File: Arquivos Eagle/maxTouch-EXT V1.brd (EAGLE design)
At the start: 35.6 x 53.3 mm, 14 parts

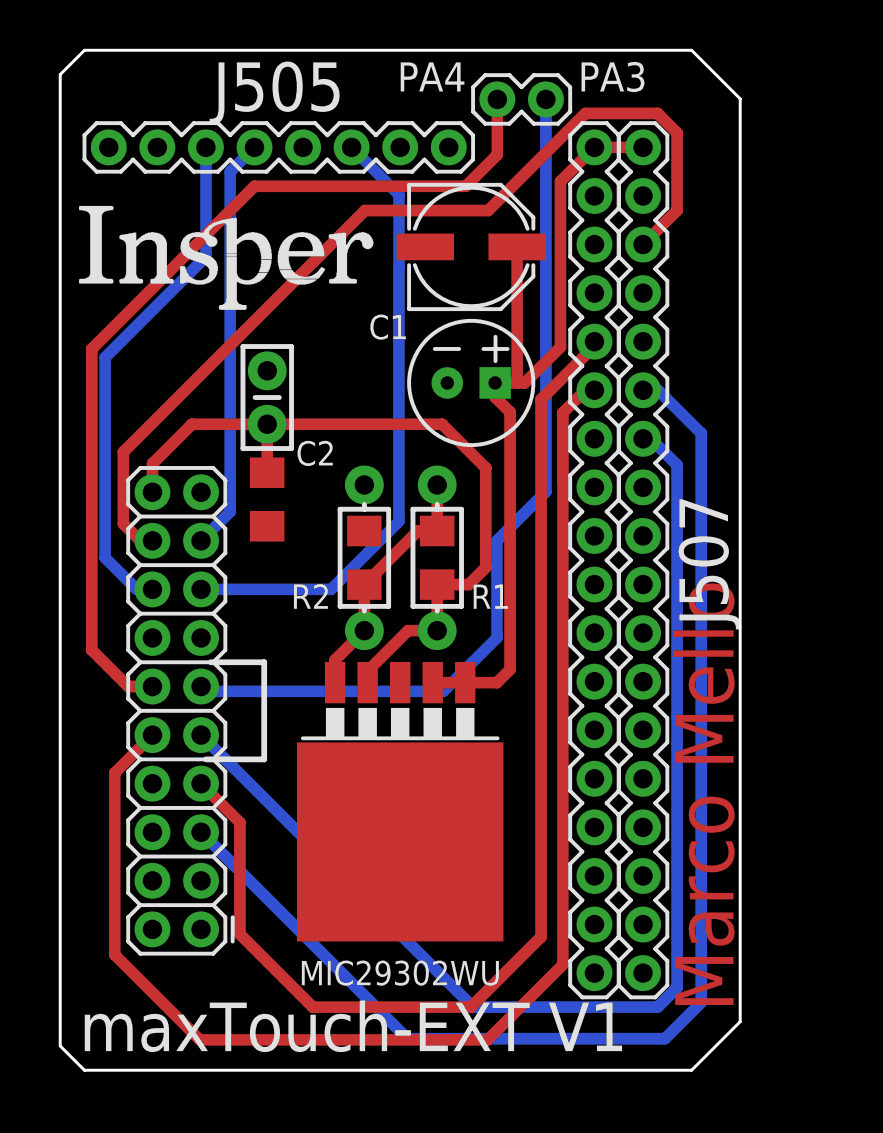
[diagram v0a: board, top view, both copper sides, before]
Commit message: Alterado o regulador para obter todos os componentes no Brasil
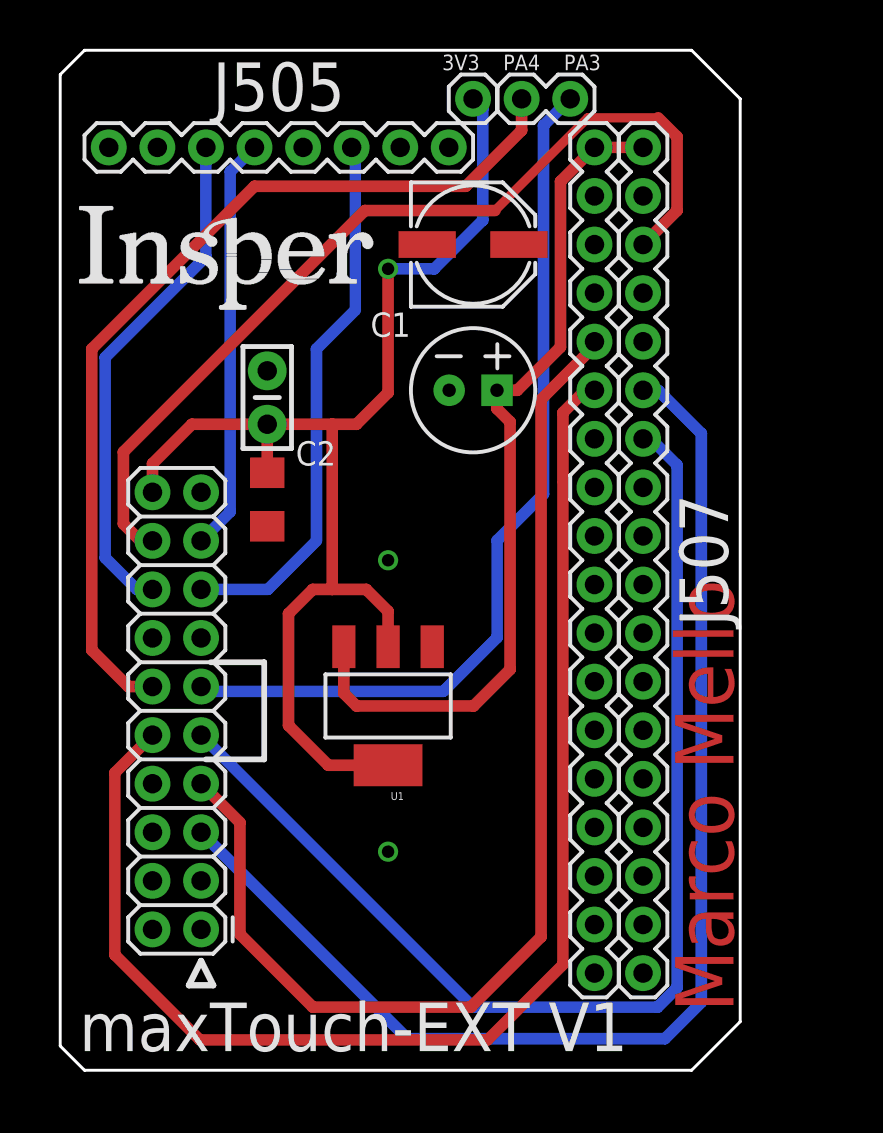
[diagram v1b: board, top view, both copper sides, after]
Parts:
- removed MIC29302WU: MIC29502BT, stepper_drivers_etc:TO263-5
- removed R1: 160R, SparkFun-Resistors:1206
- removed R2: 100R, SparkFun-Resistors:1206
- removed R3: 160R, SparkFun-Resistors:AXIAL-0.3-KIT
- removed R4: 100R, SparkFun-Resistors:AXIAL-0.3-KIT
- added J6: (no value), SparkFun-Connectors:1X01
- added U1: (no value), SparkFun-IC-Power:SOT223
- moved J5 1.27 mm to (26.7, 50.8)
- moved C3 0.39 mm to (21.6, 35.6)
- moved C1 0.16 mm to (21.6, 43.2)
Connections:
- removed net N$2: MIC29302WU.5, R1.1, R2.2, R3.P$1, R4.P$2
- net 3V3: now also J6.1, U1.2, U1.4; no longer MIC29302WU.4, R1.2, R3.P$2
- net 5V: now also U1.3; no longer MIC29302WU.1, MIC29302WU.2
- net GND: now also U1.1; no longer MIC29302WU.3, MIC29302WU.6, R2.1, R4.P$1
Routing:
- net 3V3: track 38.9 -> 65.5 mm, vias 0 -> 1
- net N$2: track 13.1 -> 0.00 mm
- net CS: track 32.4 -> 28.6 mm
- net SDA: track 46.0 -> 46.5 mm
- net SCL: track 48.0 -> 48.6 mm
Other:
- board text added: "3V3"

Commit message: ~
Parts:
- C2: device SparkFun-Capacitors:1206 -> SparkFun-Capacitors:0805
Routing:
- net 3V3: track 65.5 -> 66.0 mm
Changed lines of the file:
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@@
 <attribute name="PROD_ID" value="CAP-12547" x="21.59" y="43.18" size="1.778" layer="27" display="off"/>
 </element>
-<element name="C2" library="SparkFun-Capacitors" package="1206" value="10uF" x="10.826" y="29.846" smashed="yes" rot="R270">
+<element name="C2" library="SparkFun-Capacitors" package="0805" value="10uF" x="10.826" y="29.846" smashed="yes" rot="R270">
 <attribute name="NAME" x="13.366" y="32.259" size="1.27" layer="21" font="vector" ratio="20" align="center"/>
 </element>
@@
 <wire x1="10.826" y1="33.783" x2="6.889" y2="33.783" width="0.6096" layer="1"/>
 <wire x1="6.889" y1="33.783" x2="4.826" y2="31.72" width="0.6096" layer="1"/>
-<wire x1="10.826" y1="31.246" x2="10.826" y2="33.783" width="0.6096" layer="1"/>
+<wire x1="10.826" y1="30.746" x2="10.826" y2="33.783" width="0.6096" layer="1"/>
 <contactref element="U1" pad="4"/>
 <contactref element="U1" pad="2"/>

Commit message: Pequenas Alterações no .brd
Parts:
- C1: device SparkFun-Capacitors:PANASONIC_D -> SparkFun-Capacitors:NIC_10X10.5_CAP
- moved C1 2.87 mm to (18.8, 42.5)
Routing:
- net 5V: track 45.1 -> 47.9 mm
- net 3V3: track 66.0 -> 64.6 mm
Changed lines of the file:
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@@
 <attribute name="VALUE" x="27.94" y="52.832" size="0.6096" layer="27" font="vector" ratio="20" rot="R180"/>
 </element>
-<element name="C1" library="SparkFun-Capacitors" package="PANASONIC_D" value="100uF" x="21.59" y="43.18" smashed="yes">
-<attribute name="NAME" x="17.272" y="38.989" size="1.27" layer="21" font="vector" ratio="20" align="center"/>
-<attribute name="PROD_ID" value="CAP-12547" x="21.59" y="43.18" size="1.778" layer="27" display="off"/>
+<element name="C1" library="SparkFun-Capacitors" package="NIC_10X10.5_CAP" value="100uF" x="18.796" y="42.545" smashed="yes">
+<attribute name="NAME" x="14.478" y="38.354" size="1.27" layer="21" font="vector" ratio="20" align="center"/>
+<attribute name="PROD_ID" value="CAP-08362" x="18.796" y="42.545" size="1.778" layer="27" display="off"/>
 </element>
 <element name="C2" library="SparkFun-Capacitors" package="0805" value="10uF" x="10.826" y="29.846" smashed="yes" rot="R270">
@@
 <via x="17.145" y="26.67" extent="1-16" drill="0.65"/>
 <via x="17.145" y="11.43" extent="1-16" drill="0.65"/>
+<wire x1="14.296" y1="42.545" x2="10.826" y2="36.577" width="0" layer="19" extent="1-1"/>
 </signal>
 <signal name="PWM">
@@
 <wire x1="30.48" y1="43.18" x2="32.258" y2="44.958" width="0.6096" layer="1"/>
 <wire x1="32.258" y1="48.8188" x2="31.2674" y2="49.8094" width="0.6096" layer="1"/>
-<wire x1="27.589" y1="49.8094" x2="22.7376" y2="44.958" width="0.4826" layer="1"/>
-<wire x1="22.7376" y1="44.958" x2="15.93141875" y2="44.958" width="0.6096" layer="1"/>
+<wire x1="27.589" y1="49.8094" x2="22.7988" y2="45.0192" width="0.4826" layer="1"/>
+<wire x1="22.7988" y1="45.0192" x2="22.7376" y2="44.958" width="0.4826" layer="1"/>
 <wire x1="3.302" y1="28.575" x2="4.191" y2="27.686" width="0.6096" layer="1"/>
 <wire x1="4.191" y1="27.686" x2="4.826" y2="27.686" width="0.6096" layer="1"/>
 <wire x1="32.258" y1="44.958" x2="32.258" y2="48.8188" width="0.6096" layer="1"/>
 <wire x1="31.2674" y1="49.8094" x2="27.589" y2="49.8094" width="0.4826" layer="1"/>
-<wire x1="15.93141875" y1="44.958" x2="3.302" y2="32.32858125" width="0.6096" layer="1"/>
+<wire x1="9.680209375" y1="38.706790625" x2="3.302" y2="32.32858125" width="0.6096" layer="1"/>
 <wire x1="3.302" y1="32.32858125" x2="3.302" y2="28.575" width="0.6096" layer="1"/>
+<wire x1="22.7988" y1="45.0192" x2="21.5242" y2="45.0192" width="0.6096" layer="1"/>
+<wire x1="21.5242" y1="45.0192" x2="15.211790625" y2="38.706790625" width="0.6096" layer="1"/>
+<wire x1="15.211790625" y1="38.706790625" x2="9.680209375" y2="38.706790625" width="0.6096" layer="1"/>
 </signal>
 <signal name="3V3">
@@
 <wire x1="10.826" y1="33.783" x2="14.224" y2="33.783" width="0.6096" layer="1"/>
 <wire x1="15.494" y1="33.783" x2="14.224" y2="33.783" width="0.6096" layer="1"/>
-<via x="17.145" y="41.91" extent="1-16" drill="0.65"/>
+<via x="17.145" y="35.687" extent="1-16" drill="0.65"/>
 <wire x1="17.145" y1="15.951" x2="14.021" y2="15.951" width="0.6096" layer="1"/>
 <wire x1="14.021" y1="15.951" x2="11.938" y2="18.034" width="0.6096" layer="1"/>
@@
 <wire x1="21.59" y1="50.8" x2="22.098" y2="50.292" width="0.6096" layer="16"/>
 <wire x1="22.098" y1="44.45" x2="22.098" y2="50.292" width="0.6096" layer="16"/>
-<wire x1="17.145" y1="41.91" x2="17.145" y2="35.434" width="0.6096" layer="1"/>
+<wire x1="17.145" y1="35.687" x2="17.145" y2="35.434" width="0.6096" layer="1"/>
 <wire x1="17.145" y1="35.434" x2="15.494" y2="33.783" width="0.6096" layer="1"/>
-<wire x1="17.145" y1="41.91" x2="19.558" y2="41.91" width="0.6096" layer="16"/>
-<wire x1="19.558" y1="41.91" x2="22.098" y2="44.45" width="0.6096" layer="16"/>
+<wire x1="17.145" y1="35.687" x2="17.145" y2="39.497" width="0.6096" layer="16"/>
+<wire x1="17.145" y1="39.497" x2="22.098" y2="44.45" width="0.6096" layer="16"/>
 </signal>
 <signal name="5V">
@@
 <contactref element="C3" pad="1"/>
 <wire x1="27.94" y1="48.26" x2="26.162" y2="46.482" width="0.6096" layer="1"/>
-<wire x1="26.162" y1="46.482" x2="26.162" y2="37.816" width="0.6096" layer="1"/>
+<wire x1="26.162" y1="46.482" x2="26.162" y2="42.545" width="0.6096" layer="1"/>
 <contactref element="U1" pad="3"/>
+<wire x1="26.162" y1="42.545" x2="26.162" y2="37.816" width="0.6096" layer="1"/>
 <wire x1="23.526" y1="33.909" x2="23.526" y2="20.956" width="0.6096" layer="1"/>
 <wire x1="14.8336" y1="19.7104" x2="14.8336" y2="22.1488" width="0.6096" layer="1"/>
@@
 <wire x1="22.84" y1="35.56" x2="22.84" y2="34.595" width="0.6096" layer="1"/>
 <wire x1="22.84" y1="34.595" x2="23.526" y2="33.909" width="0.6096" layer="1"/>
-<wire x1="27.94" y1="48.26" x2="23.99" y2="43.18" width="0" layer="19" extent="1-1"/>
+<wire x1="23.296" y1="42.545" x2="26.162" y2="42.545" width="0.6096" layer="1"/>
 </signal>
 <signal name="PD19">

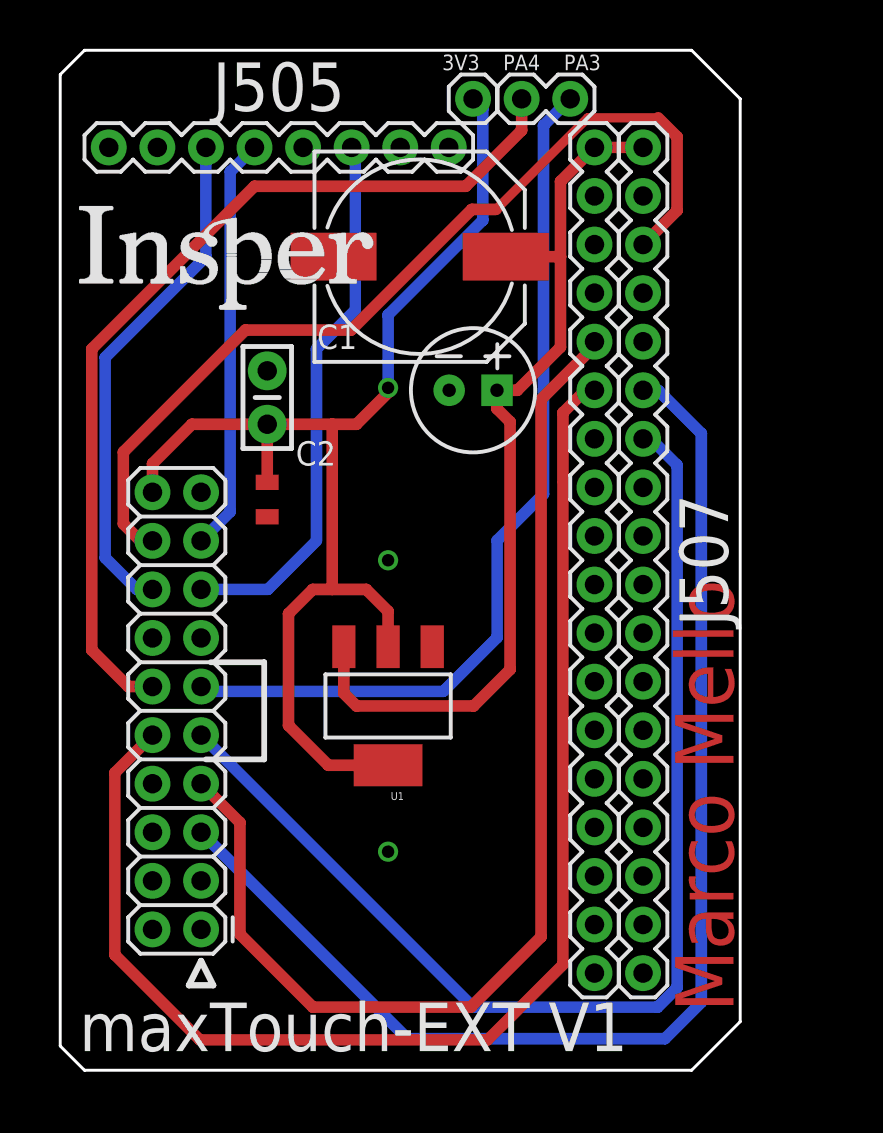
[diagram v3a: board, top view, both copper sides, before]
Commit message: Pequenas alteracoes no Layout
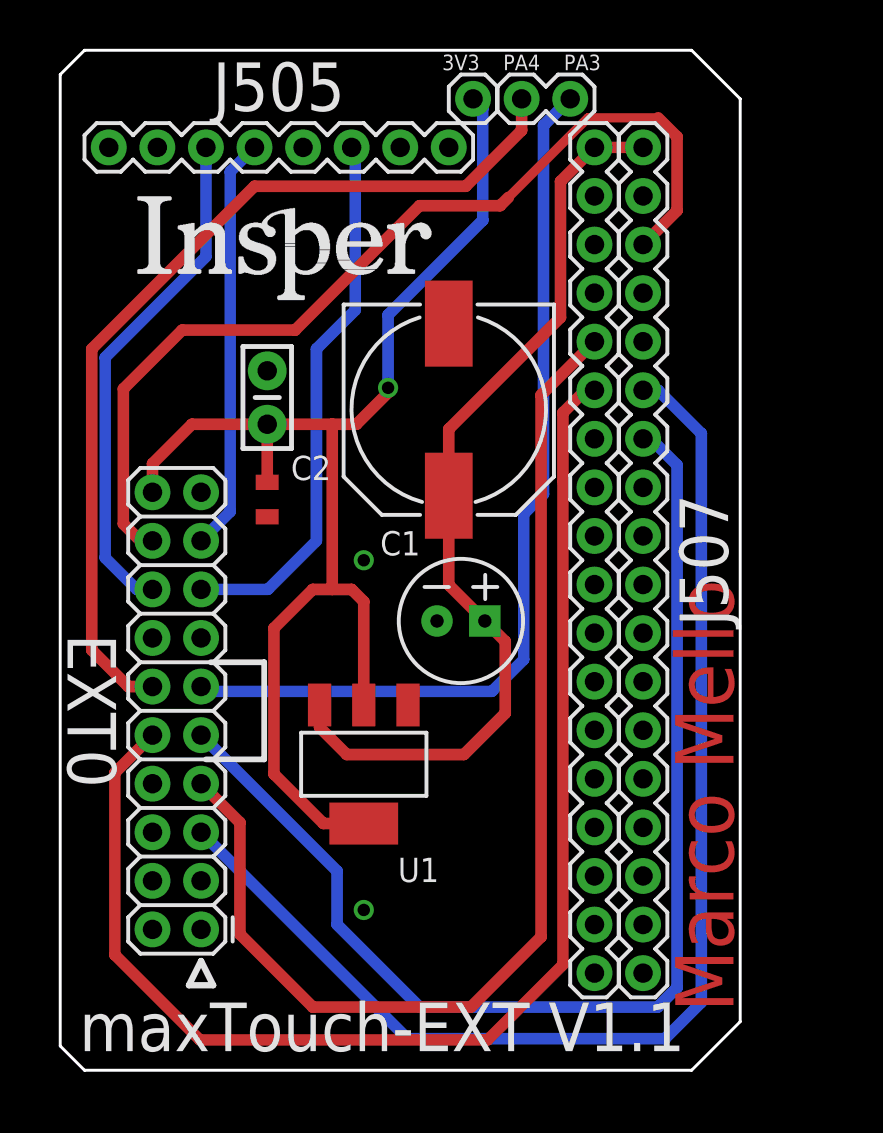
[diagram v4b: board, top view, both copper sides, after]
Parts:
- C3: value 100uF -> 100UF-POLAR-RADIAL-2.5MM-25V-20%
- C4: value 0.1uF -> 0.1UF-KIT-EZ-50V-20%
- moved C3 12.1 mm to (21.0, 23.5)
- moved C1 8.14 mm to (20.3, 34.5), turned to 270 degrees
- moved U1 3.30 mm to (15.9, 16.0)
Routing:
- net 3V3: track 64.6 -> 69.3 mm
- net SCK: track 48.7 -> 50.6 mm
- net IRQ: track 60.9 -> 62.5 mm
- net SDA: track 46.5 -> 48.0 mm
- net 5V: track 47.9 -> 48.9 mm
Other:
- board text added: "EXT0"
- board text added: "maxTouch-EXT V1.1"
- board text removed: "maxTouch-EXT V1"
